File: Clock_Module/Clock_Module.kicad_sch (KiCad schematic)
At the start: 29 parts, among them J1 PC104, SW1 Switch, U1 74LS08, U2 74LS32, U3 74LS04, U4 LM555xN, U5 LM555xN, U6 LM555xN

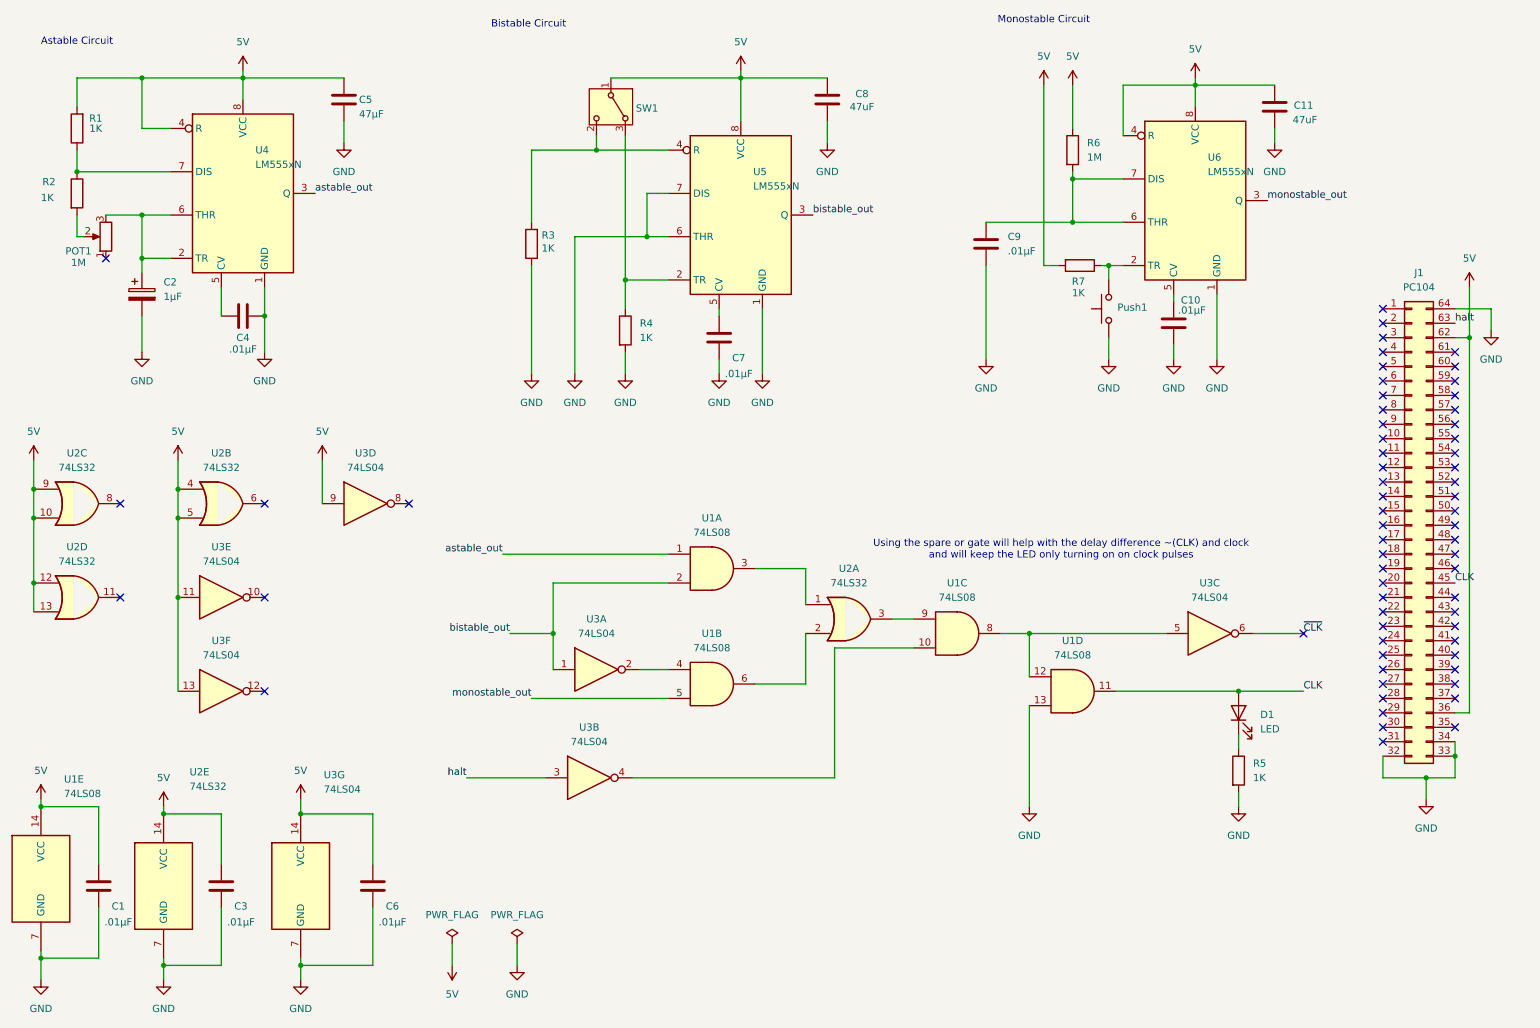
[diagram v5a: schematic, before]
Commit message: Updated Clock Module Schematic, and moved Instruction Register to new board
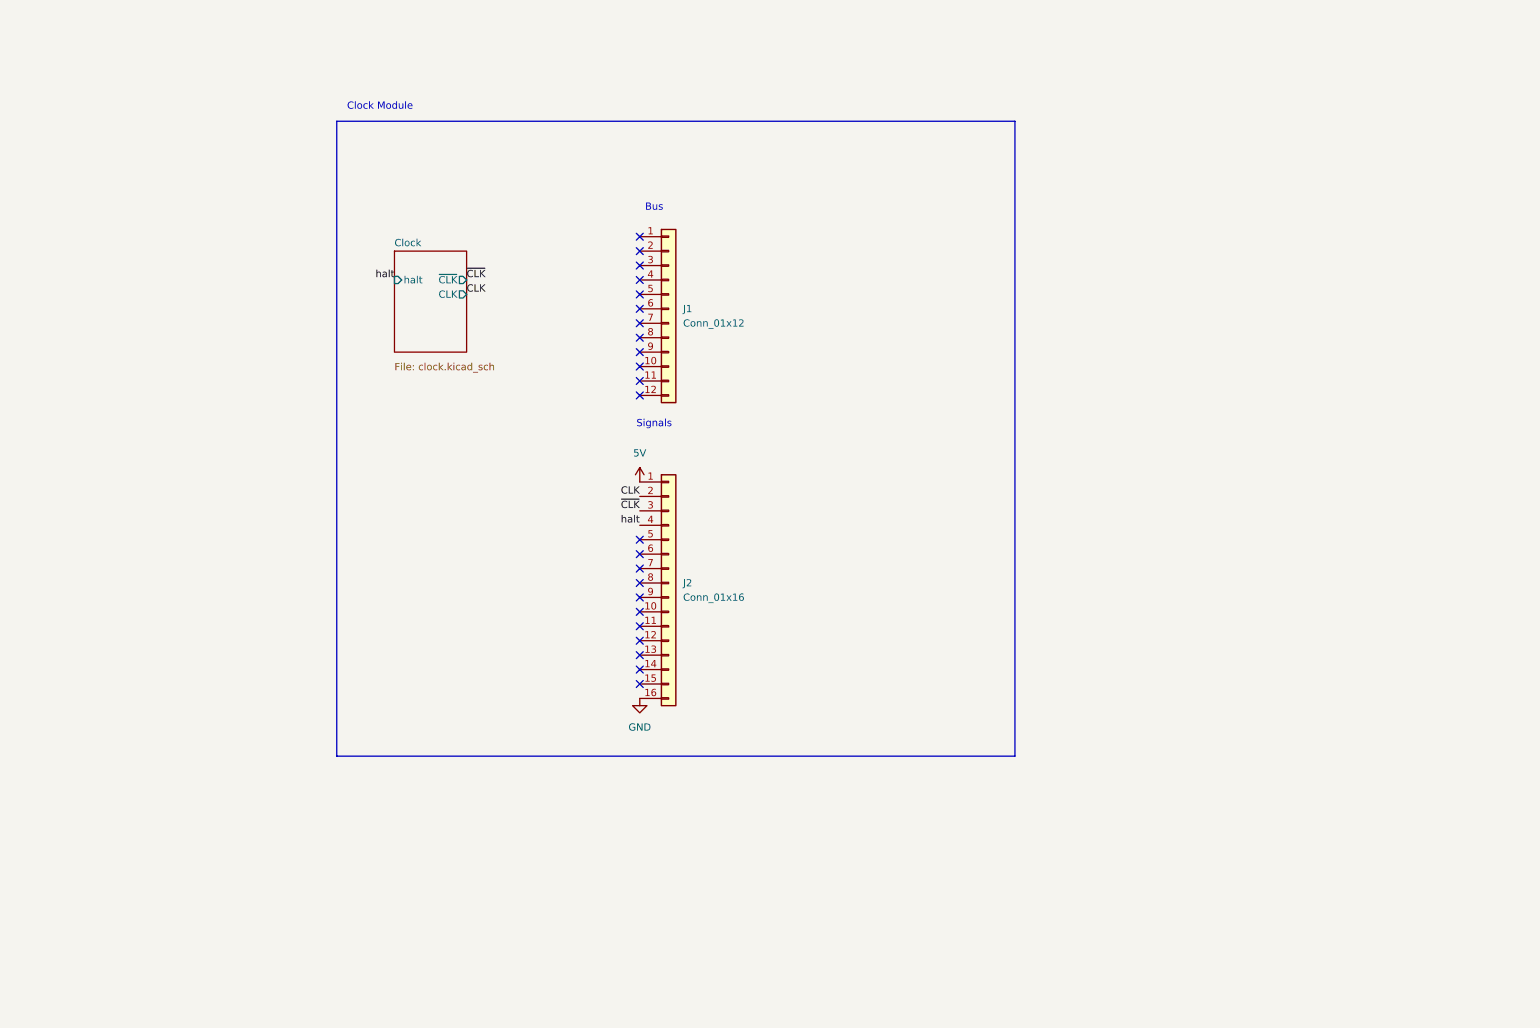
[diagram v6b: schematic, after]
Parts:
- removed C1, C10, C3, C4, C6, C7, C9: .01µF, Capacitor_THT:C_Disc_D5.0mm_W2.5mm_P2.50mm, symbol Device:C
- removed C11, C8: 47uF, Capacitor_THT:C_Disc_D5.0mm_W2.5mm_P2.50mm, symbol Device:C
- removed C2: 1µF, Capacitor_THT:C_Radial_D5.0mm_H11.0mm_P2.00mm, symbol Device:C_Polarized
- removed C5: 47µF, Capacitor_THT:C_Disc_D5.0mm_W2.5mm_P2.50mm, symbol Device:C
- removed D1: LED, LED_THT:LED_D5.0mm, symbol Device:LED
- removed J1: PC104, Connector_PinSocket_2.54mm:PinSocket_2x32_P2.54mm_Vertical, symbol Connector_Generic:Conn_02x32_Counter_Clockwise
- removed POT1: 1M, Potentiometer_THT:Potentiometer_Bourns_3386F_Vertical, symbol Device:R_Potentiometer
- removed Push1: SW_Push, Button_Switch_THT:SW_PUSH_6mm_H4.3mm, symbol Switch:SW_Push
- removed R1, R2, R3, R4, R5, R7: 1K, Resistor_THT:R_Axial_DIN0207_L6.3mm_D2.5mm_P5.08mm_Vertical, symbol Device:R
- removed R6: 1M, Resistor_THT:R_Axial_DIN0207_L6.3mm_D2.5mm_P5.08mm_Vertical, symbol Device:R
- removed SW1: Switch, MyFootPrints:SW_Slide-Jameco-SS-12E17-G020, symbol Switch:SW_Wuerth_450301014042
- removed U1: 74LS08, MyFootPrints:SN74LS08N, symbol 74xx:74LS08
- removed U2: 74LS32, MyFootPrints:SN74LS32N, symbol 74xx:74LS32
- removed U3: 74LS04, MyFootPrints:SN74LS04N, symbol 74xx:74LS04
- removed U4, U5, U6: LM555xN, Package_DIP:DIP-8_W7.62mm, symbol Timer:LM555xN
- added J1: Conn_01x12, Connector_PinSocket_2.54mm:PinSocket_1x12_P2.54mm_Vertical, symbol Connector_Generic:Conn_01x12
- added J2: Conn_01x16, Connector_PinSocket_2.54mm:PinSocket_1x16_P2.54mm_Vertical, symbol Connector_Generic:Conn_01x16
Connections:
- net 5V: now also J2.1 (Pin_1)
- net CLK: now also J2.2 (Pin_2)
- net GND: now also J2.16 (Pin_16)
- net halt: now also J2.4 (Pin_4)
- net ~{CLK}: now also J2.3 (Pin_3)
- no-connect marks 64 -> 23
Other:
- added sheet Clock (clock.kicad_sch)
- note added: "Bus"
- note added: "Clock Module"
- note added: "Signals"
- note removed: "Astable Circuit"
- note removed: "Bistable Circuit"
- note removed: "Monostable Circuit"
- note removed: "Using the spare or gate will help with the delay difference ~(CLK) and clock and will keep the LED only turning on on clock pulses"

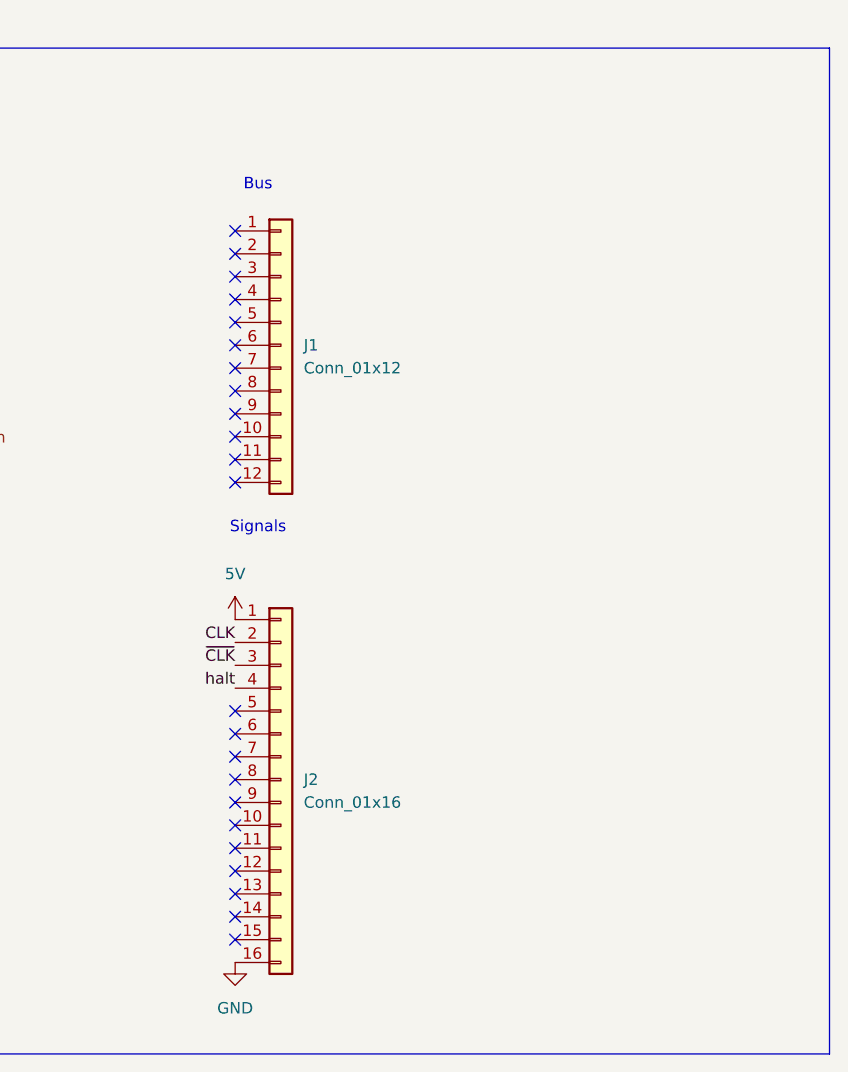
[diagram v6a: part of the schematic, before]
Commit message: returning to pc104 standard
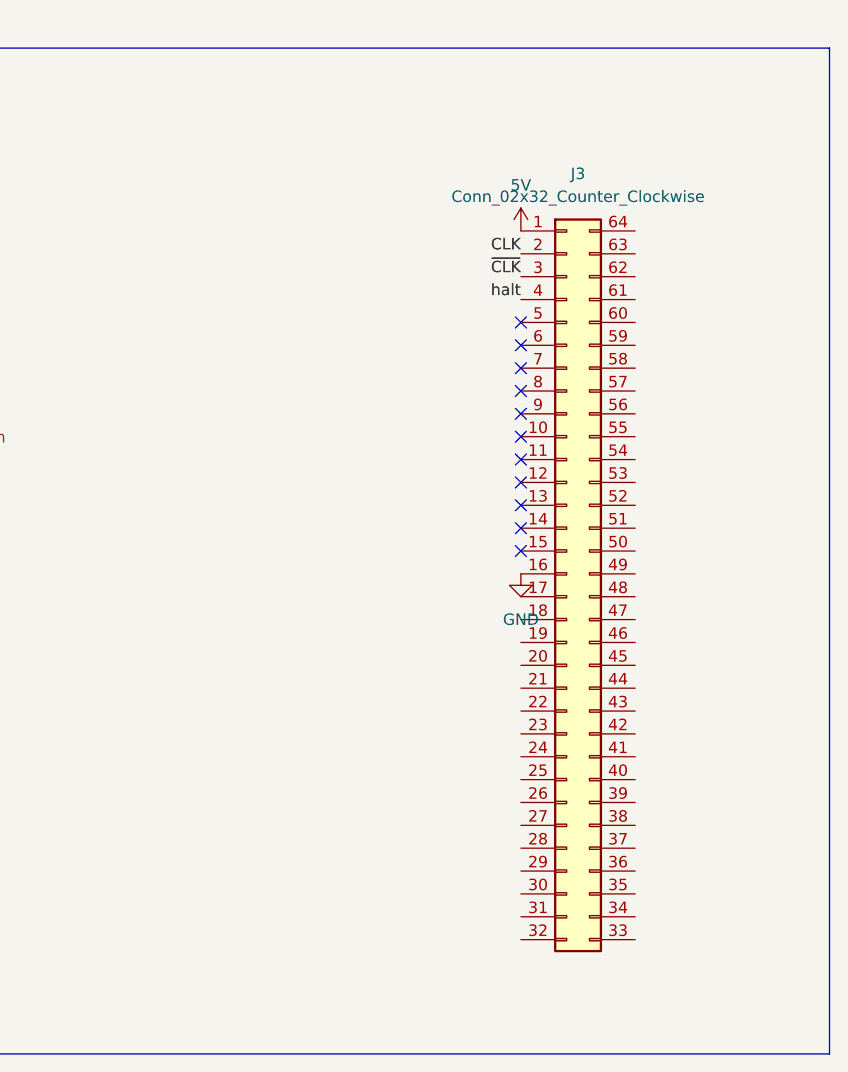
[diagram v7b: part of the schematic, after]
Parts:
- removed J1: Conn_01x12, Connector_PinSocket_2.54mm:PinSocket_1x12_P2.54mm_Vertical, symbol Connector_Generic:Conn_01x12
- removed J2: Conn_01x16, Connector_PinSocket_2.54mm:PinSocket_1x16_P2.54mm_Vertical, symbol Connector_Generic:Conn_01x16
- added J3: Conn_02x32_Counter_Clockwise, MyFootPrints:PC104-Standard, symbol Connector_Generic:Conn_02x32_Counter_Clockwise
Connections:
- net 5V: now also J3.1 (Pin_1)
- net CLK: now also J3.2 (Pin_2)
- net GND: now also J3.16 (Pin_16)
- net halt: now also J3.4 (Pin_4)
- net ~{CLK}: now also J3.3 (Pin_3)
- no-connect marks 23 -> 11
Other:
- note removed: "Bus"
- note removed: "Signals"

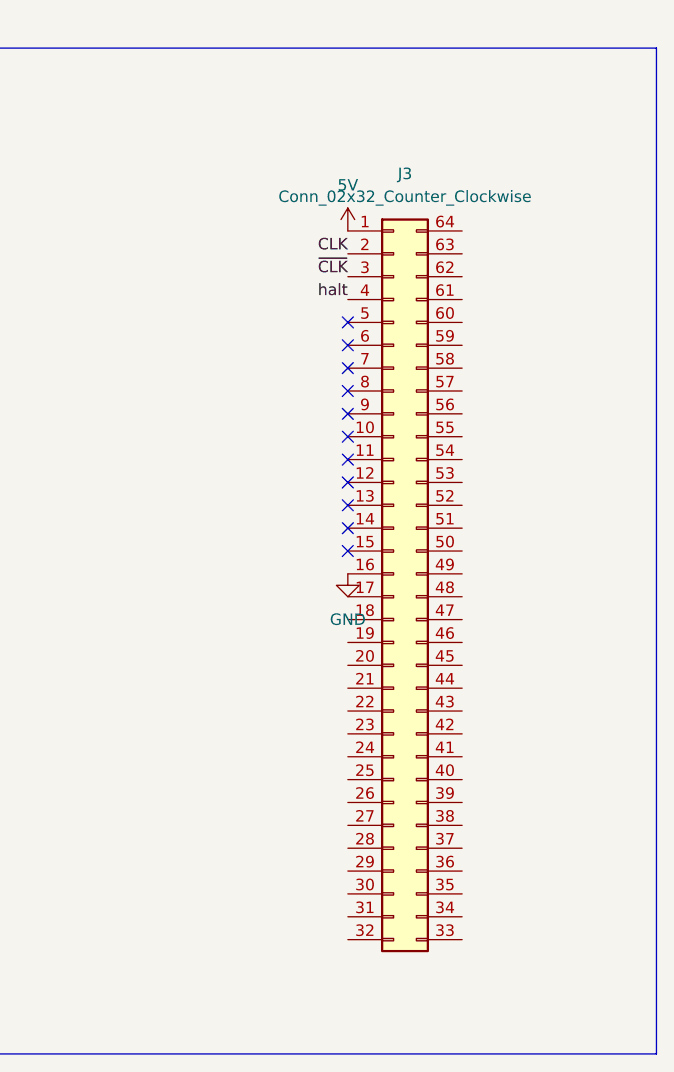
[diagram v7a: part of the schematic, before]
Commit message: fixed clock module, made it back into pc104 board standard
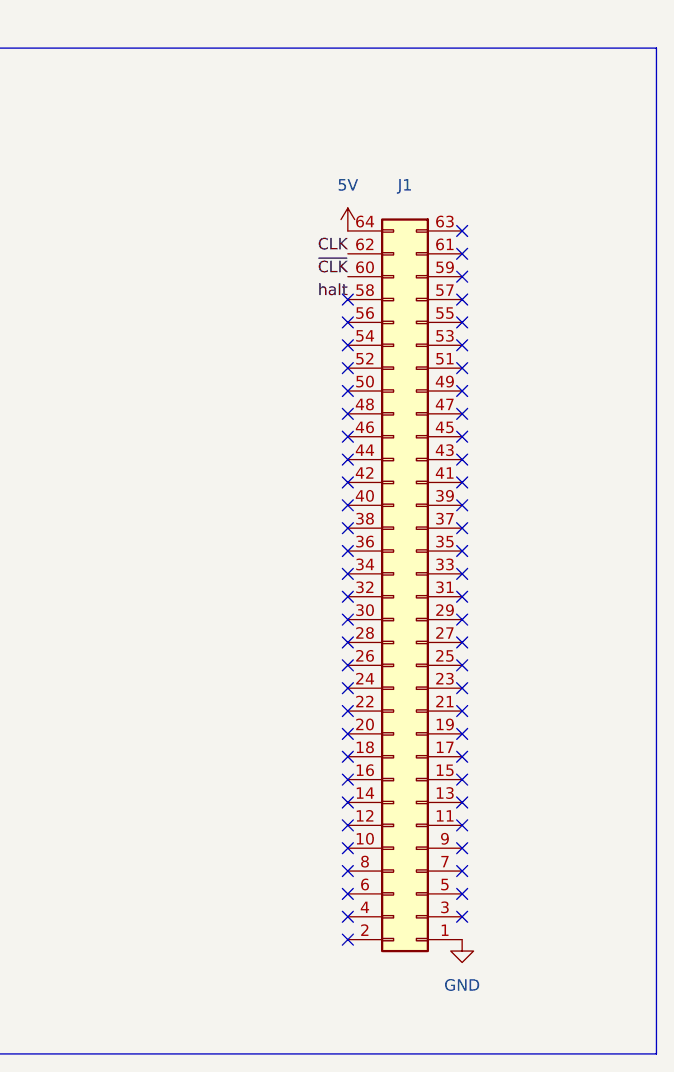
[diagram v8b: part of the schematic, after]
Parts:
- removed J3: Conn_02x32_Counter_Clockwise, MyFootPrints:PC104-Standard, symbol Connector_Generic:Conn_02x32_Counter_Clockwise
- added J1: ~, MyFootPrints:PC104-Standard, symbol pc104:PC104
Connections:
- net 5V: now also J1.64
- net CLK: now also J1.62
- net GND: now also J1.1
- net halt: now also J1.58
- net ~{CLK}: now also J1.60
- no-connect marks 11 -> 60
